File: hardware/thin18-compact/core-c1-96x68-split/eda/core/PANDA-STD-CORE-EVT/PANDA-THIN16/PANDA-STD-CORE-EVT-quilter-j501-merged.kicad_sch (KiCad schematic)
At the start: 125 parts, among them J301 HC-HY-2AWT, J501 TF-122-CCP9 / microSD, J502 HC-1.0-2PWT BTL, J503 TC2030-IDC-NL / DEBUG, J803 X05A10H06G, SW201 TS-1186E-B-B, SW202 TS-1186E-B-B, U301 BQ27427YZFR, U302 SD3078, U402 SGM2578SDYG/TR, U403 SGM2578SDYG/TR, U404 SGM2578SDYG/TR, U405 SGM2578SDYG/TR, U501 ESP32-S3-WROOM-1U-N16R8, U502 MAX98357AETE+T, U503 QMI8658A, U601 XL9535, U901 SGM41513YTQF24G/TR, U902 SGM62125AXG/TR, U903 CW2217BAAD, U904 NS4168

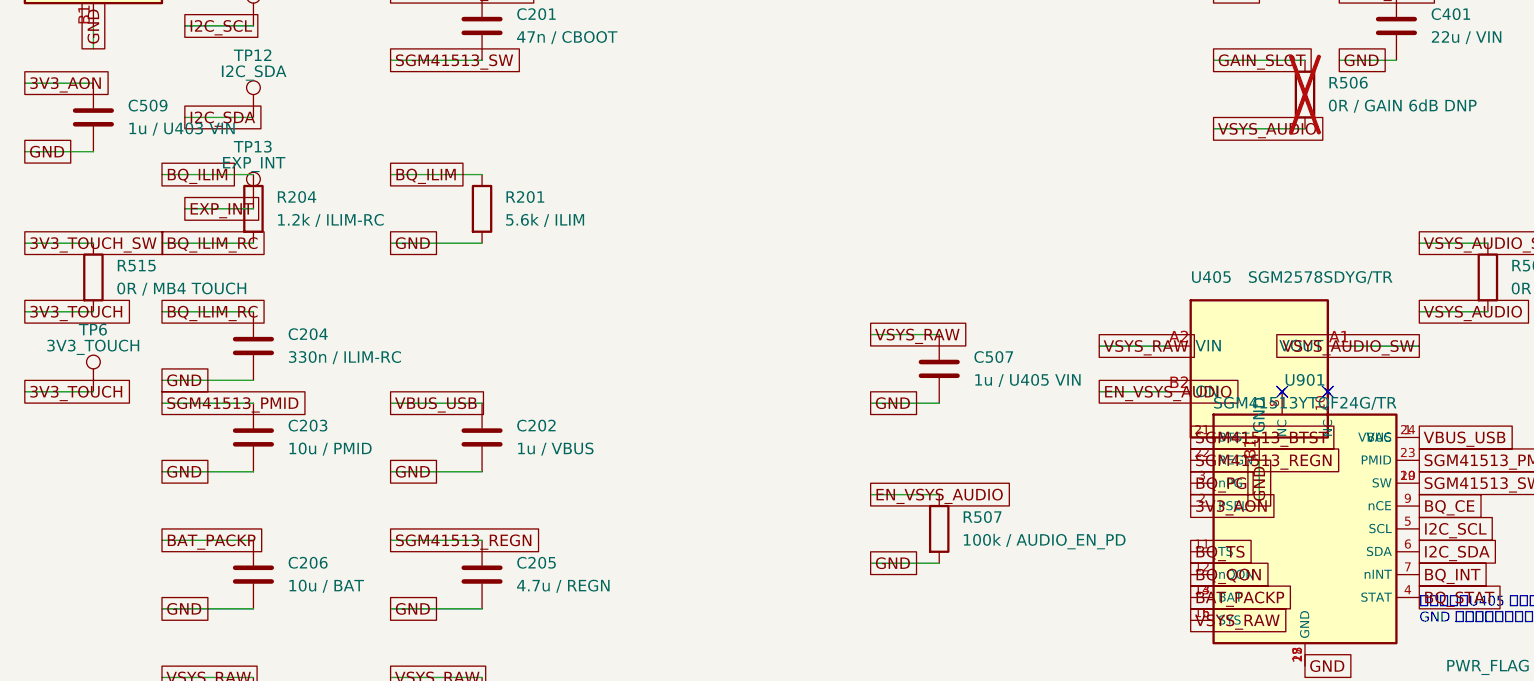
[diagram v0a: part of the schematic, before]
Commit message: hw: implement Split-C1 PG monitor and pre-AON PSEL bias
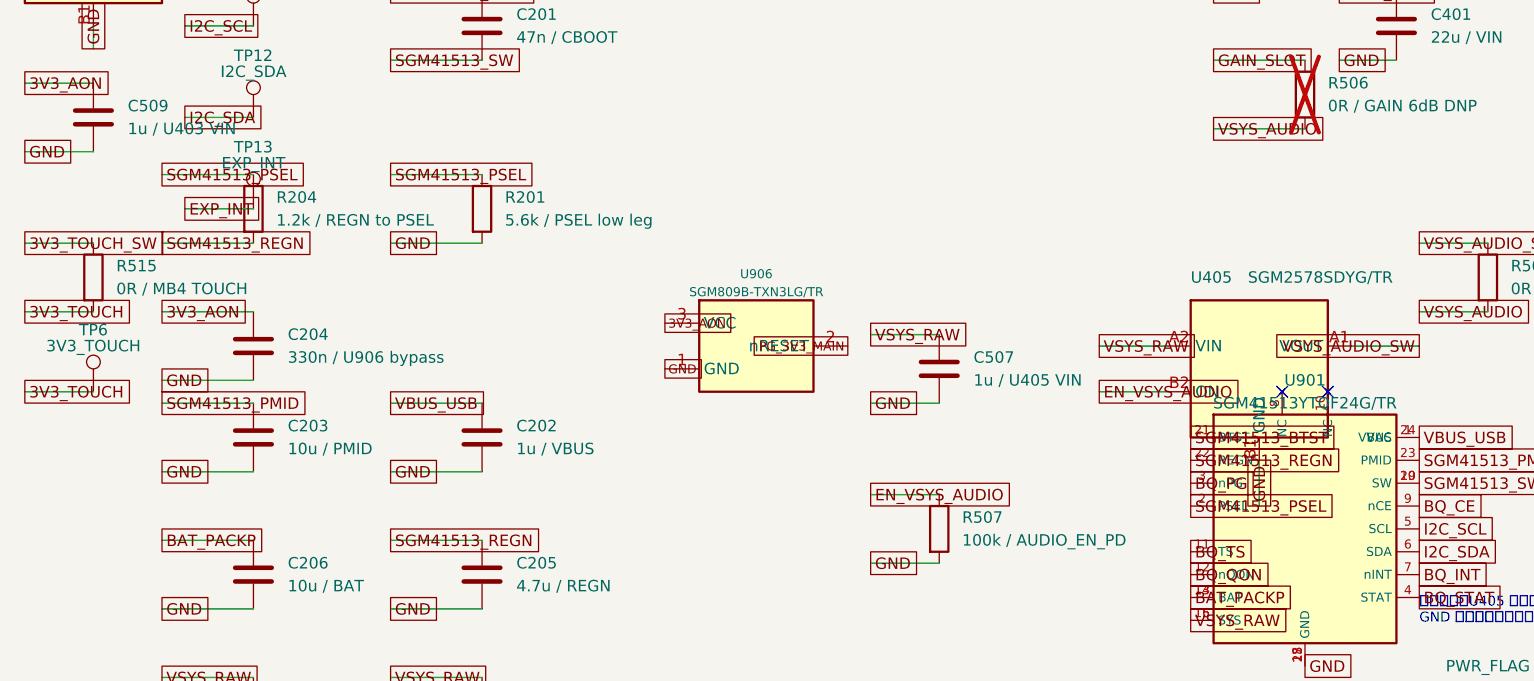
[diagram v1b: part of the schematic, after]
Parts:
- added U906: SGM809B-TXN3LG/TR, panda-standard:SGM809B_SOT23_TX00031, symbol panda-standard:SGM809B_TXN3LG_TR
- C204: value 330n / ILIM-RC -> 330n / U906 bypass
- R201: value 5.6k / ILIM -> 5.6k / PSEL low leg
- R204: value 1.2k / ILIM-RC -> 1.2k / REGN to PSEL
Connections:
- net 3V3_AON: now also C204.1, U906.3 (VCC); no longer U901.2 (PSEL)
- net GND: now also U906.1 (GND)
- net PG_3V3_MAIN: now also U906.2 (nRESET)
- net SGM41513_REGN: now also R204.2
- net BQ_ILIM renamed SGM41513_PSEL
- net SGM41513_PSEL: now also U901.2 (PSEL)
- removed net BQ_ILIM_RC: C204.1, R204.2

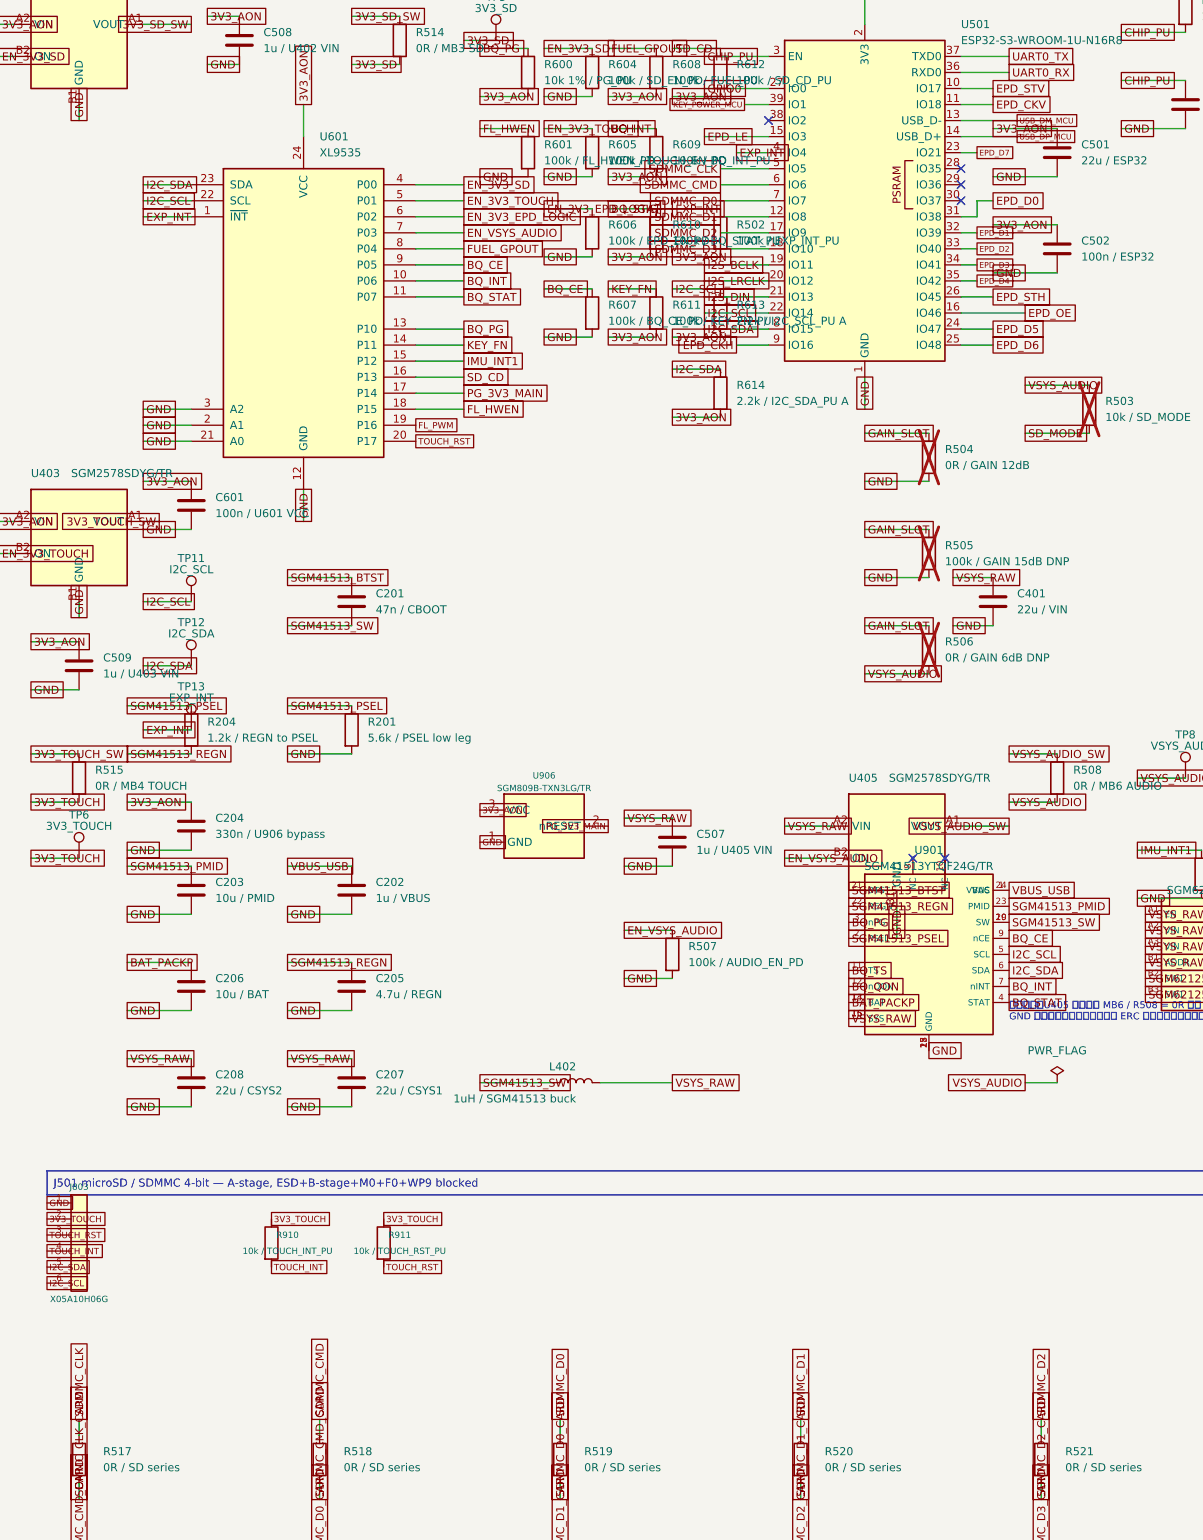
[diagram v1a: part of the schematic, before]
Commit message: hw: finish Split-C1 default-off charging and direct GPIO inhibit
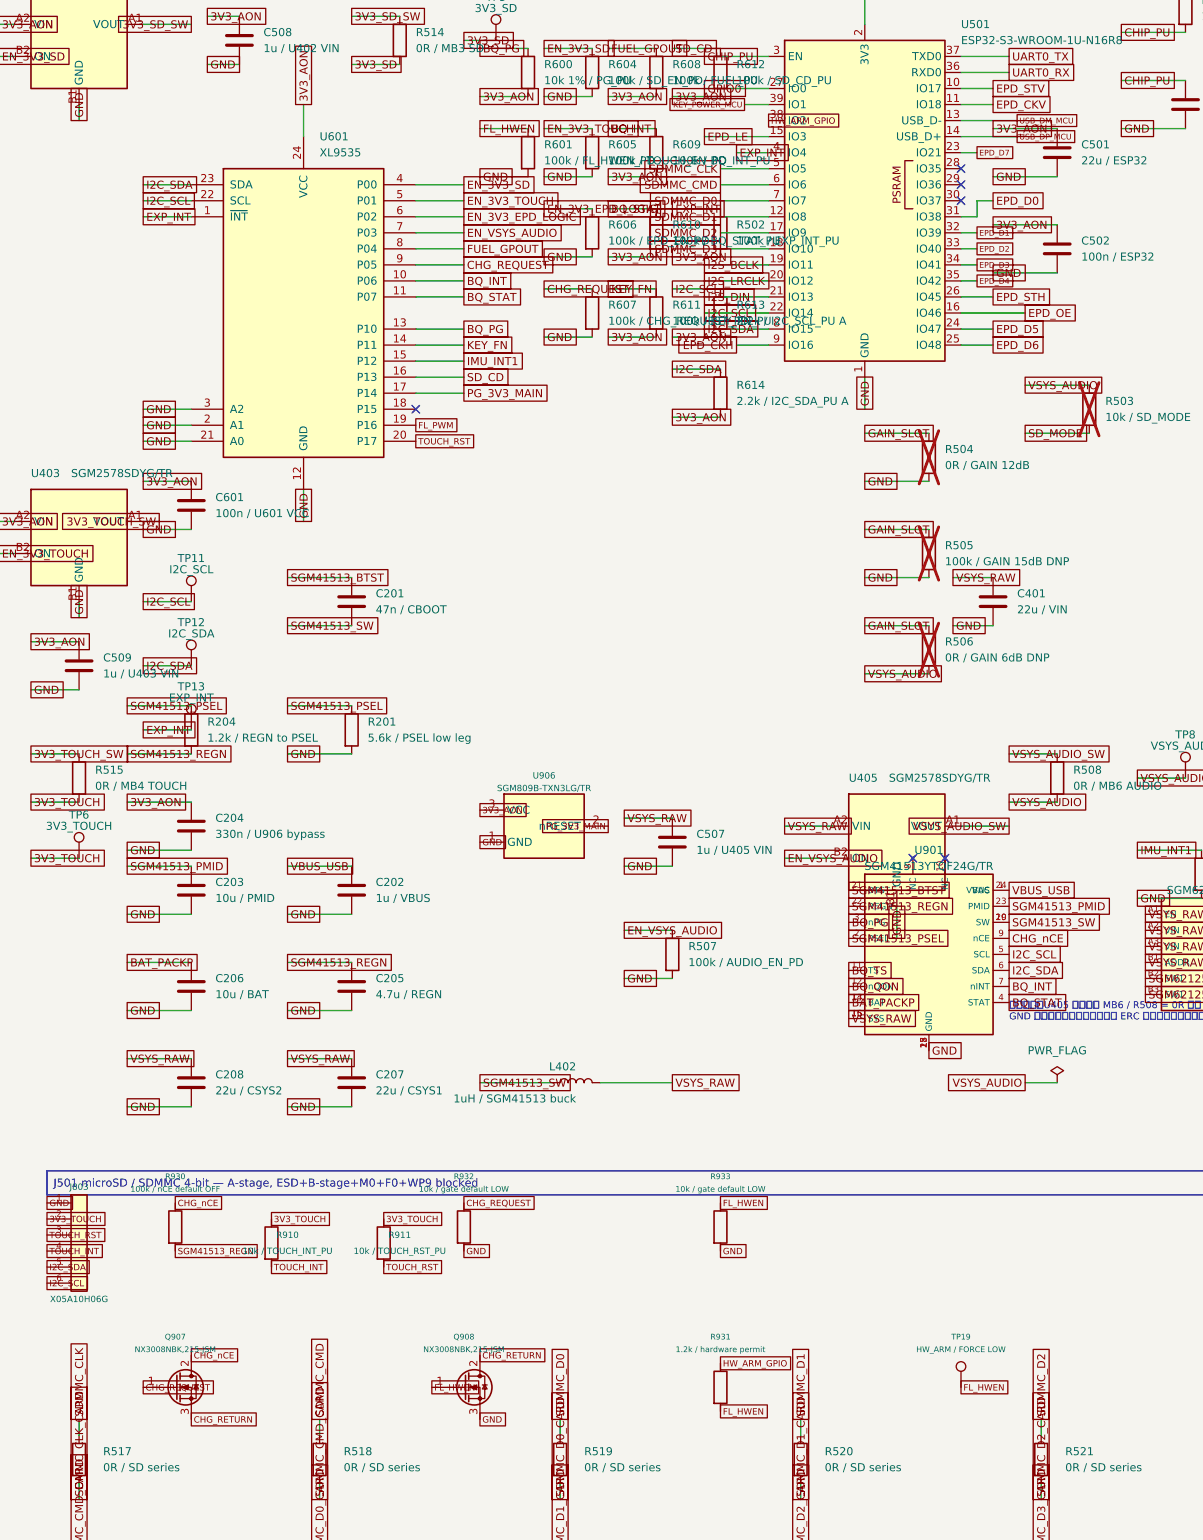
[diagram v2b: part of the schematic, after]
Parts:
- added Q907, Q908: NX3008NBK,215-JSM, panda-standard:JSM_NX3008NBK_SOT23, symbol panda-standard:NX3008NBK_215_JSM
- added R930: 100k / nCE default OFF, Resistor_SMD:R_0402_1005Metric, symbol Device:R
- added R931: 1.2k / hardware permit, panda-standard:R204_ILIM_RC_0603_SEED, symbol Device:R
- added R932, R933: 10k / gate default LOW, Resistor_SMD:R_0402_1005Metric, symbol Device:R
- added TP19: HW_ARM / FORCE LOW, TestPoint:TestPoint_Pad_D1.5mm, symbol Connector:TestPoint
- R607: value 100k / BQ_CE_PD -> 100k / CHG_REQUEST_PD
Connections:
- net FL_HWEN: now also Q908.1 (G), R931.2, R933.1, TP19.1; no longer U601.18 (P15)
- net GND: now also Q908.3 (S), R932.2, R933.2
- net SGM41513_REGN: now also R930.2
- net HW_ARM_GPIO: now reaches U501.38 (IO2)
- net HW_ARM_GPIO: now also R931.1
- net BQ_CE renamed CHG_REQUEST
- net CHG_REQUEST: now also Q907.1 (G), R932.1; no longer U901.9 (nCE)
- new net CHG_RETURN: Q907.3 (S), Q908.2 (D)
- new net CHG_nCE: Q907.2 (D), R930.1, U901.9 (nCE)

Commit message: hw: close reviewed via escapes and supervisor sourcing on develop
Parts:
- U906: LCSC (none) -> C699619
